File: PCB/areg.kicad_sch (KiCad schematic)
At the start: 14 parts, among them J3 AREG, Q10 2N3906, Q9 2N5457, U2 LM324

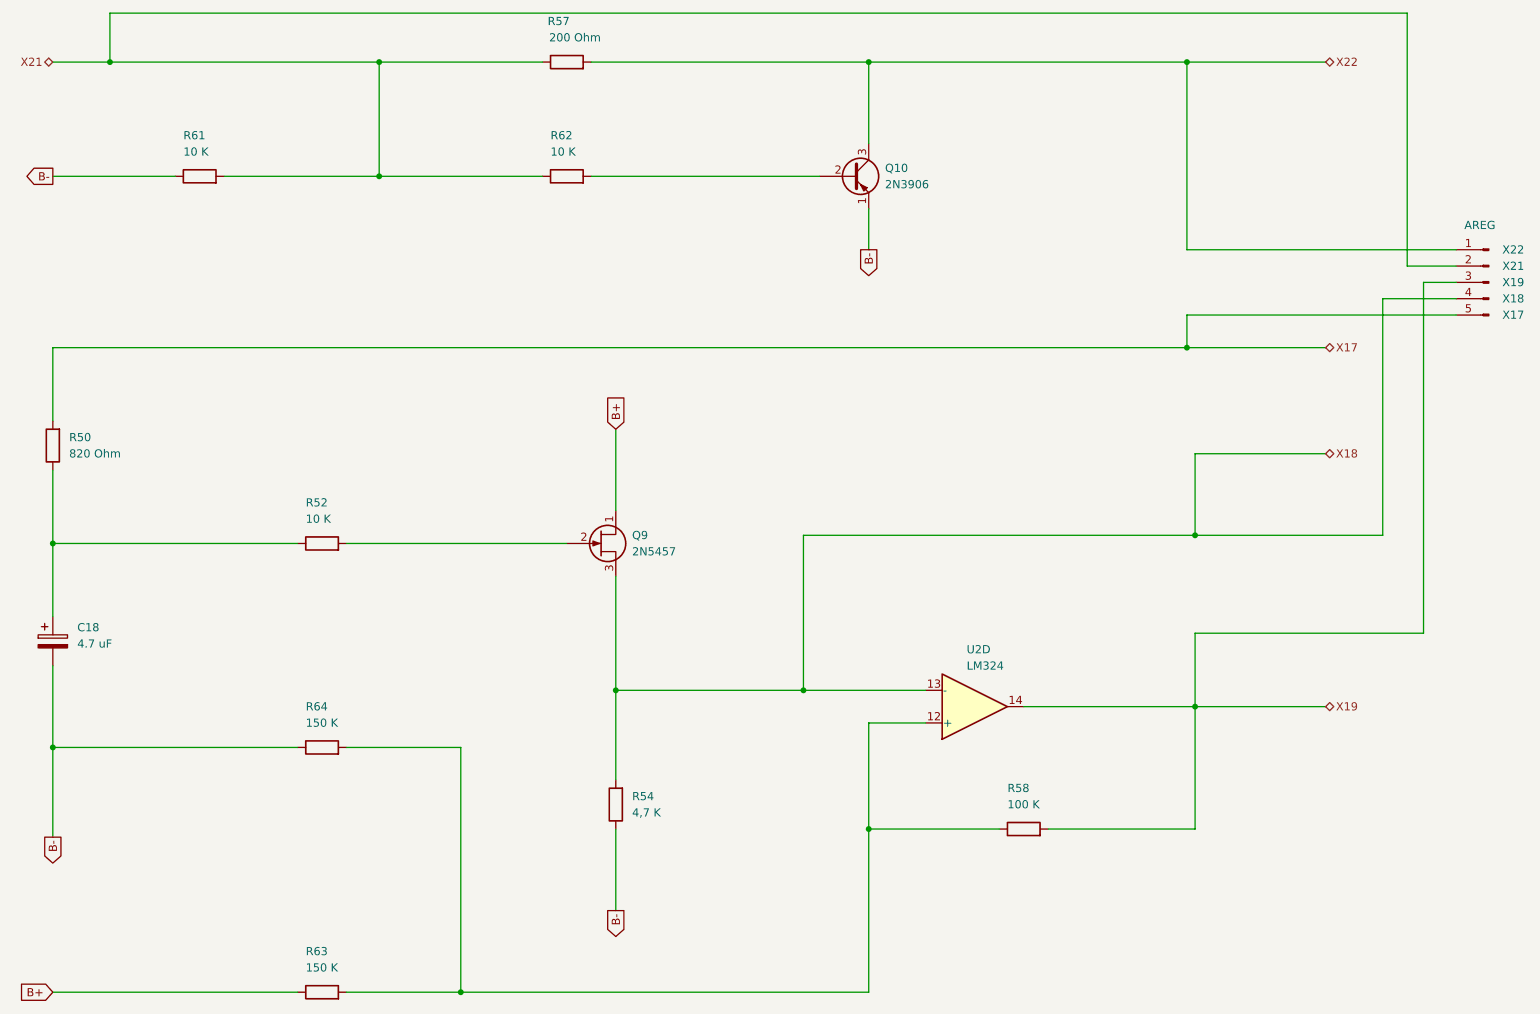
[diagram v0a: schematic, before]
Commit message: Change TO-92 transistors to wide package to avoid shorting during soldering
Added B- hole for speaker
Added more vias to shorten traces
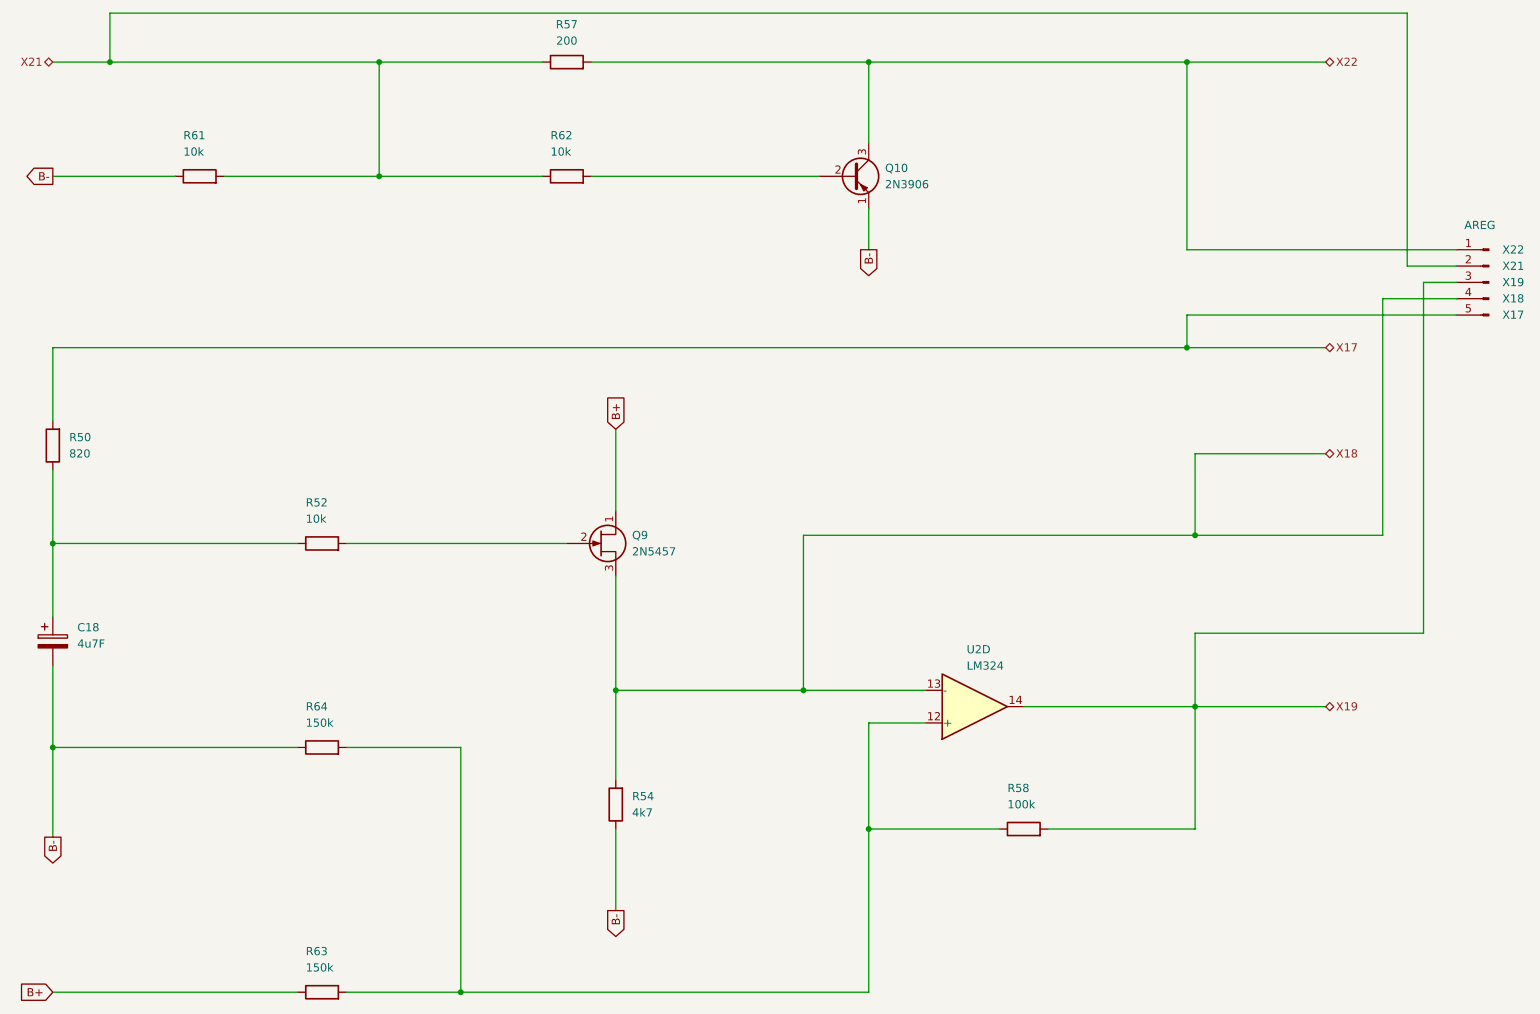
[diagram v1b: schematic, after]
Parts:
- C18: value 4.7 uF -> 4u7F
- R50: value 820 Ohm -> 820
- R52, R61, R62: value 10 K -> 10k
- R54: value 4,7 K -> 4k7
- R57: value 200 Ohm -> 200
- R58: value 100 K -> 100k
- R63, R64: value 150 K -> 150k
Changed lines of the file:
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@@
 		(fields_autoplaced yes)
 		(property "Reference" "C18"
-			(at 41.91 121.031 0)
+			(at 41.91 121.0309 0)
 			(show_name no)
 			(do_not_autoplace no)
@@
 			)
 		)
-		(property "Value" "4.7 uF"
-			(at 41.91 123.571 0)
+		(property "Value" "4u7F"
+			(at 41.91 123.5709 0)
 			(show_name no)
 			(do_not_autoplace no)
@@
 			)
 		)
-		(property "Value" "10 K"
+		(property "Value" "10k"
 			(at 58.42 46.99 90)
 			(show_name no)
@@
 		(fields_autoplaced yes)
 		(property "Reference" "R50"
-			(at 40.64 91.44 0)
-			(show_name no)
-			(do_not_autoplace no)
-			(effects
-				(font
-					(size 1.27 1.27)
-				)
-				(justify right)
-			)
-		)
-		(property "Value" "820 Ohm"
-			(at 40.64 93.98 0)
+			(at 40.64 91.4399 0)
+			(show_name no)
+			(do_not_autoplace no)
+			(effects
+				(font
+					(size 1.27 1.27)
+				)
+				(justify right)
+			)
+		)
+		(property "Value" "820"
+			(at 40.64 93.9799 0)
 			(show_name no)
 			(do_not_autoplace no)
@@
 			)
 		)
-		(property "Value" "150 K"
+		(property "Value" "150k"
 			(at 77.47 135.89 90)
 			(show_name no)
@@
 		(fields_autoplaced yes)
 		(property "Reference" "R54"
-			(at 128.27 147.32 0)
-			(show_name no)
-			(do_not_autoplace no)
-			(effects
-				(font
-					(size 1.27 1.27)
-				)
-				(justify right)
-			)
-		)
-		(property "Value" "4,7 K"
-			(at 128.27 149.86 0)
+			(at 128.27 147.3199 0)
+			(show_name no)
+			(do_not_autoplace no)
+			(effects
+				(font
+					(size 1.27 1.27)
+				)
+				(justify right)
+			)
+		)
+		(property "Value" "4k7"
+			(at 128.27 149.8599 0)
 			(show_name no)
 			(do_not_autoplace no)
@@
 			)
 		)
-		(property "Value" "10 K"
+		(property "Value" "10k"
 			(at 77.47 104.14 90)
 			(show_name no)
@@
 			)
 		)
-		(property "Value" "10 K"
+		(property "Value" "10k"
 			(at 115.57 46.99 90)
 			(show_name no)
@@
 			)
 		)
-		(property "Value" "100 K"
+		(property "Value" "100k"
 			(at 186.69 148.59 90)
 			(show_name no)
@@
 		(dnp no)
 		(property "Reference" "R57"
-			(at 116.84 26.67 90)
-			(show_name no)
-			(do_not_autoplace no)
-			(effects
-				(font
-					(size 1.27 1.27)
-				)
-			)
-		)
-		(property "Value" "200 Ohm"
-			(at 119.38 29.21 90)
+			(at 118.11 27.178 90)
+			(show_name no)
+			(do_not_autoplace no)
+			(effects
+				(font
+					(size 1.27 1.27)
+				)
+			)
+		)
+		(property "Value" "200"
+			(at 118.11 29.718 90)
 			(show_name no)
 			(do_not_autoplace no)
@@
 			)
 		)
-		(property "Value" "150 K"
+		(property "Value" "150k"
 			(at 77.47 173.99 90)
 			(show_name no)

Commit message: Necessary Changes to Schematic and PCB
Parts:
- C18: footprint Capacitor_THT:CP_Radial_D4.0mm_P1.50mm -> Capacitor_THT:CP_Radial_D4.0mm_P2.00mm
- J3: footprint Connector_PinHeader_2.00mm:PinHeader_1x05_P2.00mm_Vertical -> Connector_PinSocket_2.54mm:PinSocket_1x05_P2.54mm_Vertical
- Q10: footprint Package_TO_SOT_THT:TO-92_Inline -> Package_TO_SOT_THT:TO-92_Inline_Wide
- Q9: footprint Package_TO_SOT_THT:TO-92_Inline -> Package_TO_SOT_THT:TO-92_Inline_Wide; symbol Device:Q_NJFET_DGS -> Device:Q_NJFET_DSG
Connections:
- net X18: now also Q9.2 (S); no longer Q9.3 (S)
- net at R52.2: now also Q9.3 (G); no longer Q9.2 (G)
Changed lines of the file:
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@@
 			)
 		)
-		(property "Footprint" "Capacitor_THT:CP_Radial_D4.0mm_P1.50mm"
+		(property "Footprint" "Capacitor_THT:CP_Radial_D4.0mm_P2.00mm"
 			(at 39.0652 127 0)
 			(hide yes)
@@
 	)
 	(symbol
-		(lib_id "Device:Q_NJFET_DGS")
+		(lib_id "Device:Q_NJFET_DSG")
 		(at 123.19 107.95 0)
 		(unit 1)
@@
 		(fields_autoplaced yes)
 		(property "Reference" "Q9"
-			(at 128.27 106.68 0)
+			(at 128.27 106.6799 0)
 			(show_name no)
 			(do_not_autoplace no)
@@
 		)
 		(property "Value" "2N5457"
-			(at 128.27 109.22 0)
+			(at 128.27 109.2199 0)
 			(show_name no)
 			(do_not_autoplace no)
@@
 			)
 		)
-		(property "Footprint" "Package_TO_SOT_THT:TO-92_Inline"
+		(property "Footprint" "Package_TO_SOT_THT:TO-92_Inline_Wide"
 			(at 128.27 105.41 0)
 			(hide yes)
@@
 			)
 		)
-		(property "Description" ""
+		(property "Description" "N-JFET transistor, drain/source/gate"
 			(at 123.19 107.95 0)
 			(hide yes)
@@
 			)
 		)
-		(property "Footprint" "Package_TO_SOT_THT:TO-92_Inline"
+		(property "Footprint" "Package_TO_SOT_THT:TO-92_Inline_Wide"
 			(at 167.64 52.705 0)
 			(hide yes)
@@
 			)
 		)
-		(property "Footprint" "Connector_PinHeader_2.00mm:PinHeader_1x05_P2.00mm_Vertical"
+		(property "Footprint" "Connector_PinSocket_2.54mm:PinSocket_1x05_P2.54mm_Vertical"
 			(at 261.62 67.31 0)
 			(hide yes)

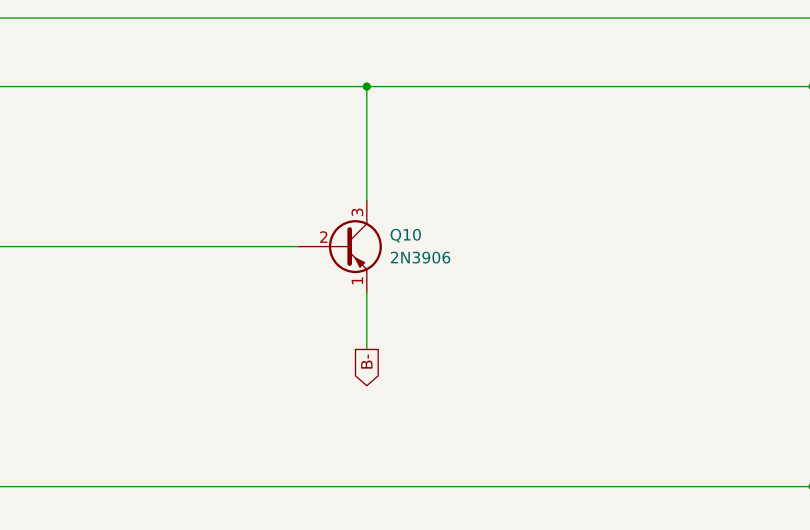
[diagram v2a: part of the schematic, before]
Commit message: Fixed grave mistake (Q10 position swapped)
Tom forgot to mirror Q10, swapping the emitter and collectors of Q10
Changed all the footprints of electrolytic caps to 5mm (i didnt find a single cap in my parts bin rated for 25V that was 4mm diameter)
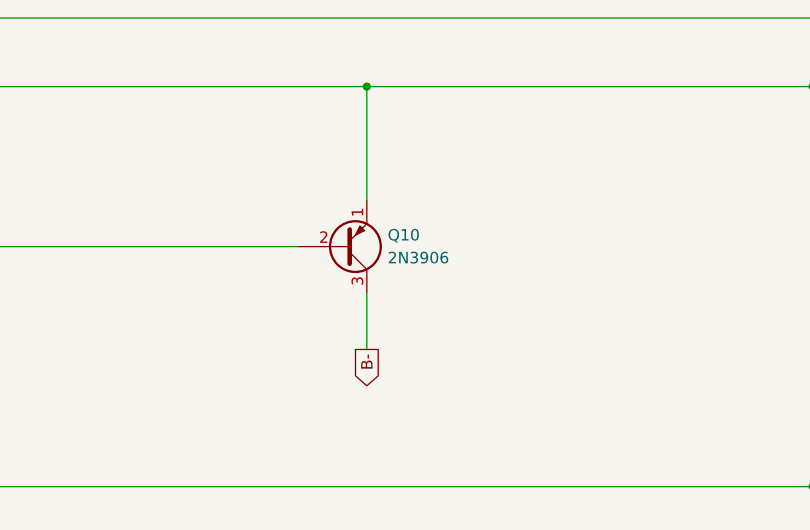
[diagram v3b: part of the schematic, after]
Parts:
- C18: footprint Capacitor_THT:CP_Radial_D4.0mm_P2.00mm -> Capacitor_THT:CP_Radial_D5.0mm_P2.00mm
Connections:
- net B-: now also Q10.3 (C); no longer Q10.1 (E)
- net X22: now also Q10.1 (E); no longer Q10.3 (C)
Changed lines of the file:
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@@
 			)
 		)
-		(property "Footprint" "Capacitor_THT:CP_Radial_D4.0mm_P2.00mm"
+		(property "Footprint" "Capacitor_THT:CP_Radial_D5.0mm_P2.00mm"
 			(at 39.0652 127 0)
 			(hide yes)
@@
 	)
 	(symbol
+		(lib_id "Transistor_BJT:2N3906")
+		(at 162.56 50.8 0)
+		(mirror x)
+		(unit 1)
+		(body_style 1)
+		(exclude_from_sim no)
+		(in_bom yes)
+		(on_board yes)
+		(in_pos_files yes)
+		(dnp no)
+		(fields_autoplaced yes)
+		(property "Reference" "Q10"
+			(at 167.4125 49.5299 0)
+			(show_name no)
+			(do_not_autoplace no)
+			(effects
+				(font
+					(size 1.27 1.27)
+				)
+				(justify left)
+			)
+		)
+		(property "Value" "2N3906"
+			(at 167.4125 52.0699 0)
+			(show_name no)
+			(do_not_autoplace no)
+			(effects
+				(font
+					(size 1.27 1.27)
+				)
+				(justify left)
+			)
+		)
+		(property "Footprint" "Package_TO_SOT_THT:TO-92_Inline_Wide"
+			(at 167.64 48.895 0)
+			(hide yes)
+			(show_name no)
+			(do_not_autoplace no)
+			(effects
+				(font
+					(size 1.27 1.27)
+					(italic yes)
+				)
+				(justify left)
+			)
+		)
+		(property "Datasheet" "https://www.onsemi.com/pub/Collateral/2N3906-D.PDF"
+			(at 162.56 50.8 0)
+			(hide yes)
+			(show_name no)
+			(do_not_autoplace no)
+			(effects
+				(font
+					(size 1.27 1.27)
+				)
+				(justify left)
+			)
+		)
+		(property "Description" ""
+			(at 162.56 50.8 0)
+			(hide yes)
+			(show_name no)
+			(do_not_autoplace no)
+			(effects
+				(font
+					(size 1.27 1.27)
+				)
+			)
+		)
+		(pin "1"
+		)
+		(pin "2"
+		)
+		(pin "3"
+		)
+		(instances
+			(project "Noise Toaster PCB"
+				(path "/7be3f398-d902-4566-9ee4-0bff072cd47e/0647ade8-e724-4924-aa52-6cbb42374298"
+					(reference "Q10")
+					(unit 1)
+				)
+			)
+		)
+	)
+	(symbol
 		(lib_id "Device:R")
 		(at 38.1 92.71 180)
@@
 					(unit 1)
 				)
-			)
-		)
-	)
-	(symbol
-		(lib_id "Transistor_BJT:2N3906")
-		(at 162.56 50.8 0)
-		(unit 1)
-		(body_style 1)
-		(exclude_from_sim no)
-		(in_bom yes)
-		(on_board yes)
-		(in_pos_files yes)
-		(dnp no)
-		(fields_autoplaced yes)
-		(property "Reference" "Q10"
-			(at 167.64 49.53 0)
-			(show_name no)
-			(do_not_autoplace no)
-			(effects
-				(font
-					(size 1.27 1.27)
-				)
-				(justify left)
-			)
-		)
-		(property "Value" "2N3906"
-			(at 167.64 52.07 0)
-			(show_name no)
-			(do_not_autoplace no)
-			(effects
-				(font
-					(size 1.27 1.27)
-				)
-				(justify left)
-			)
-		)
-		(property "Footprint" "Package_TO_SOT_THT:TO-92_Inline_Wide"
-			(at 167.64 52.705 0)
-			(hide yes)
-			(show_name no)
-			(do_not_autoplace no)
-			(effects
-				(font
-					(size 1.27 1.27)
-					(italic yes)
-				)
-				(justify left)
-			)
-		)
-		(property "Datasheet" "https://www.onsemi.com/pub/Collateral/2N3906-D.PDF"
-			(at 162.56 50.8 0)
-			(hide yes)
-			(show_name no)
-			(do_not_autoplace no)
-			(effects
-				(font
-					(size 1.27 1.27)
-				)
-				(justify left)
-			)
-		)
-		(property "Description" ""
-			(at 162.56 50.8 0)
-			(hide yes)
-			(show_name no)
-			(do_not_autoplace no)
-			(effects
-				(font
-					(size 1.27 1.27)
-				)
-			)
-		)
-		(pin "1"
-		)
-		(pin "2"
-		)
-		(pin "3"
-		)
-		(instances
-			(project "Noise Toaster PCB"
-				(path "/7be3f398-d902-4566-9ee4-0bff072cd47e/0647ade8-e724-4924-aa52-6cbb42374298"
-					(reference "Q10")
-					(unit 1)
-				)

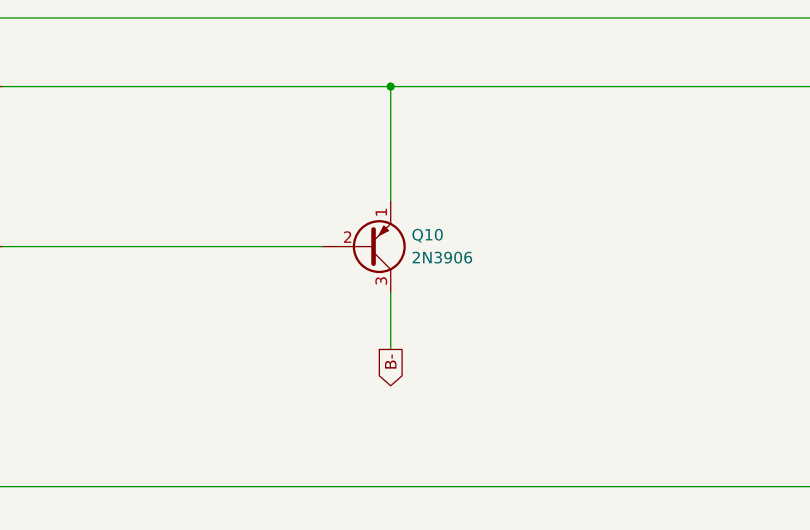
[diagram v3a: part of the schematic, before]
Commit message: Final Update
Move power pins closer to filter caps
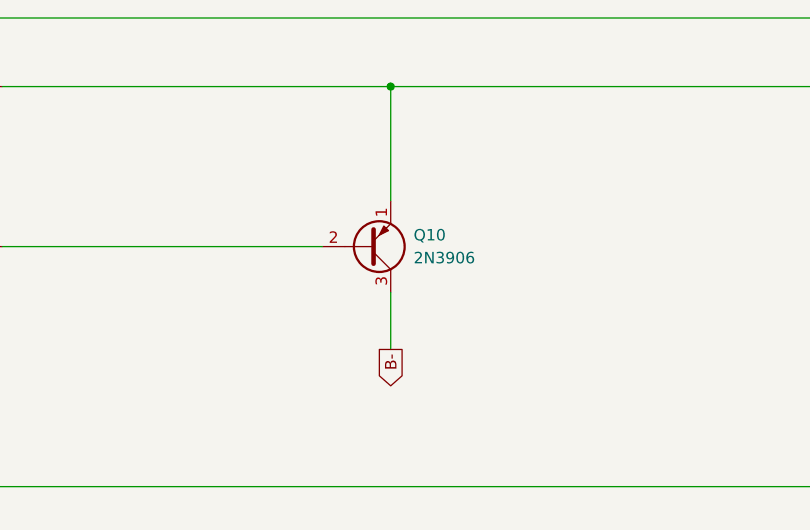
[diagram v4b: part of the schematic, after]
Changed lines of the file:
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@@
 		(fields_autoplaced yes)
 		(property "Reference" "Q10"
-			(at 167.4125 49.5299 0)
+			(at 167.64 49.5299 0)
 			(show_name no)
 			(do_not_autoplace no)
@@
 		)
 		(property "Value" "2N3906"
-			(at 167.4125 52.0699 0)
+			(at 167.64 52.0699 0)
 			(show_name no)
 			(do_not_autoplace no)
@@
 			)
 		)
-		(property "Description" ""
+		(property "Description" "-0.2A Ic, -40V Vce, Small Signal PNP Transistor, TO-92"
 			(at 162.56 50.8 0)
 			(hide yes)
+			(show_name no)
+			(do_not_autoplace no)
+			(effects
+				(font
+					(size 1.27 1.27)
+				)
+			)
+		)
+		(property "Sim.Device" "PNP"
+			(at 162.56 50.8 0)
+			(hide yes)
+			(show_name no)
+			(do_not_autoplace no)
+			(effects
+				(font
+					(size 1.27 1.27)
+				)
+			)
+		)
+		(property "Sim.Pins" "1=E 2=B 3=C"
+			(at 162.56 50.8 0)
+			(hide yes)
